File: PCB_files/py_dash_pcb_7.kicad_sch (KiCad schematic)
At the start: 5 parts, among them U1 CM4102008

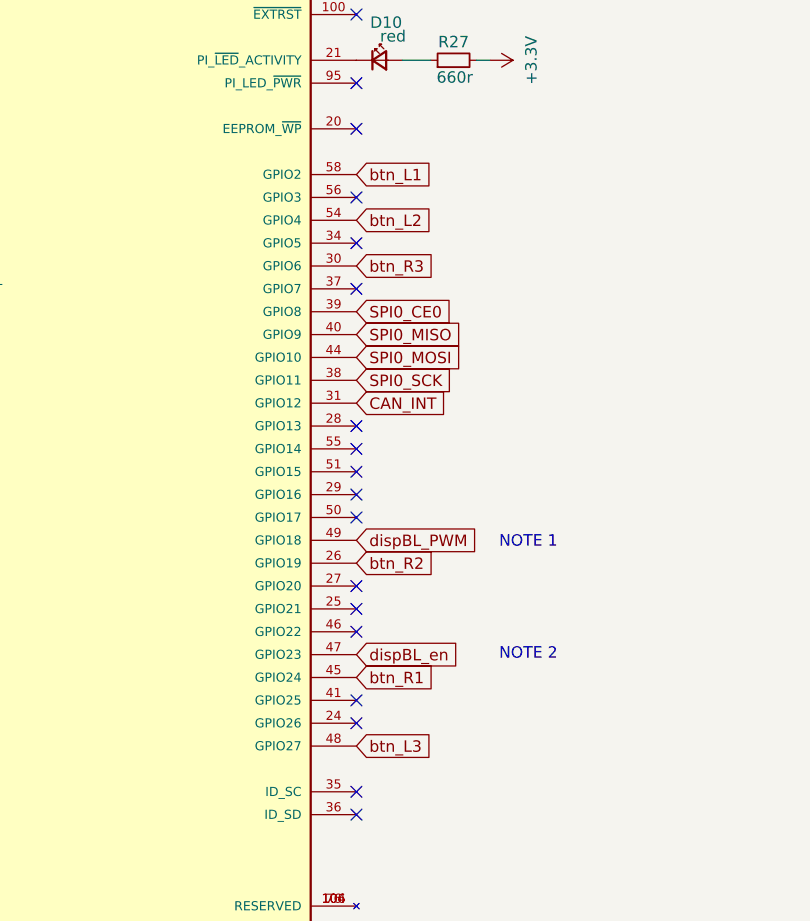
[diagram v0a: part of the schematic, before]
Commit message: r1a upload
uploaded files for r1a; correct button numbering
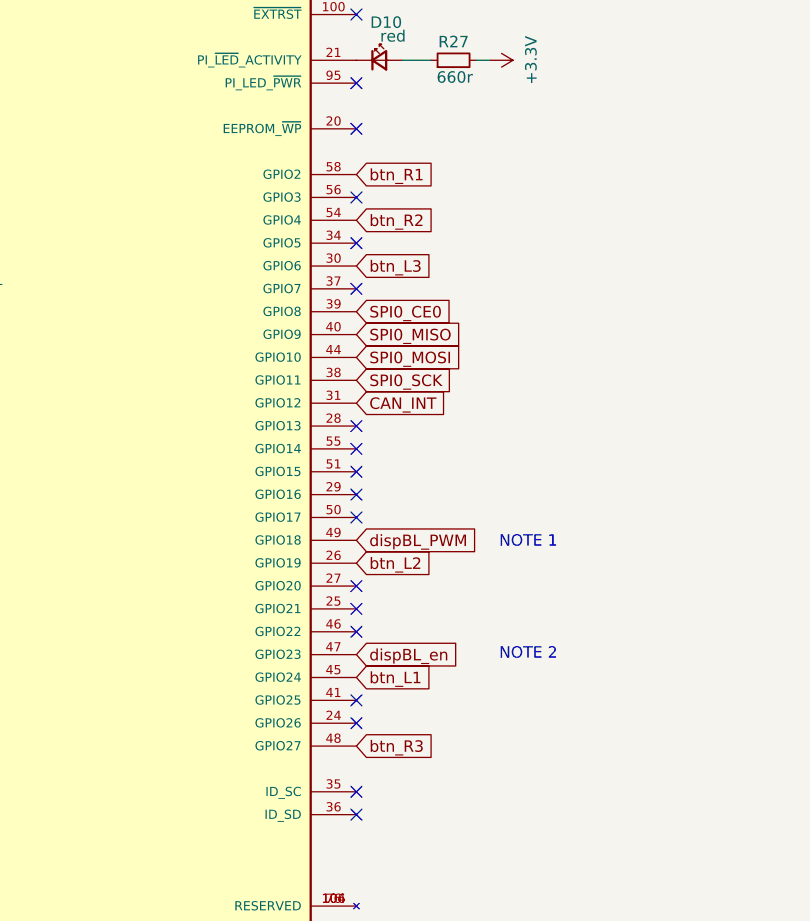
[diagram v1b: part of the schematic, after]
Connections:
- net btn_L1: now also U1.45 (GPIO24); no longer U1.58 (GPIO2)
- net btn_L2: now also U1.26 (GPIO19); no longer U1.54 (GPIO4)
- net btn_L3: now also U1.30 (GPIO6); no longer U1.48 (GPIO27)
- net btn_R1: now also U1.58 (GPIO2); no longer U1.45 (GPIO24)
- net btn_R2: now also U1.54 (GPIO4); no longer U1.26 (GPIO19)
- net btn_R3: now also U1.48 (GPIO27); no longer U1.30 (GPIO6)

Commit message: Rev2a initial upload
PCB files
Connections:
- net USB_OTG is gone; now on net GND: U1.101 (USB_OTG_ID)
- net SD_DET: now reaches U1.24 (GPIO26)
- net SD_CLK: now reaches U1.57 (SD_CLK)
- net SD_DAT3: now reaches U1.61 (SD_DAT3)
- net SD_CMD: now reaches U1.62 (SD_CMD)
- net SD_DAT0: now reaches U1.63 (SD_DAT0)
- net SD_DAT1: now reaches U1.67 (SD_DAT1)
- net SD_DAT2: now reaches U1.69 (SD_DAT2)
- net USBD+ renamed ext_USBD+
- net USBD- renamed ext_USBD-
- no-connect marks 104 -> 97

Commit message: push from desktop to align files
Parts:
- renumbered C33 to C1, C32 to C2, D10 to D1, R27 to R1
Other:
- added sheet mechanical (mechanical.kicad_sch)
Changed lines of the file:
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@@
 		(on_board yes)
 		(dnp no)
-		(property "Reference" "#PWR0101"
+		(property "Reference" "#PWR01"
 			(at 105.41 27.94 0)
 			(effects
@@
 			(project "py_dash_pcb_7"
 				(path "/84878699-1e21-48de-ad1b-9d4034e33e81"
-					(reference "#PWR0101")
+					(reference "#PWR01")
 					(unit 1)
 				)
@@
 		(on_board yes)
 		(dnp no)
-		(property "Reference" "D10"
+		(property "Reference" "D1"
 			(at 112.522 41.529 0)
 			(effects
@@
 			(project "py_dash_pcb_7"
 				(path "/84878699-1e21-48de-ad1b-9d4034e33e81"
-					(reference "D10")
+					(reference "D1")
 					(unit 1)
 				)
@@
 		(dnp no)
 		(fields_autoplaced yes)
-		(property "Reference" "#PWR0102"
+		(property "Reference" "#PWR08"
 			(at 92.837 178.562 0)
 			(effects
@@
 			(project "py_dash_pcb_7"
 				(path "/84878699-1e21-48de-ad1b-9d4034e33e81"
-					(reference "#PWR0102")
+					(reference "#PWR08")
 					(unit 1)
 				)
@@
 		(on_board yes)
 		(dnp no)
-		(property "Reference" "R27"
+		(property "Reference" "R1"
 			(at 120.015 43.688 90)
 			(effects
@@
 			(project "py_dash_pcb_7"
 				(path "/84878699-1e21-48de-ad1b-9d4034e33e81"
-					(reference "R27")
+					(reference "R1")
 					(unit 1)
 				)
@@
 		(dnp no)
 		(fields_autoplaced yes)
-		(property "Reference" "#PWR0105"
+		(property "Reference" "#PWR03"
 			(at 120.269 45.72 0)
 			(effects
@@
 			(project "py_dash_pcb_7"
 				(path "/84878699-1e21-48de-ad1b-9d4034e33e81"
-					(reference "#PWR0105")
+					(reference "#PWR03")
 					(unit 1)
 				)
@@
 		(on_board yes)
 		(dnp no)
-		(property "Reference" "#PWR0108"
+		(property "Reference" "#PWR05"
 			(at 41.91 55.88 0)
 			(effects
@@
 			(project "py_dash_pcb_7"
 				(path "/84878699-1e21-48de-ad1b-9d4034e33e81"
-					(reference "#PWR0108")
+					(reference "#PWR05")
 					(unit 1)
 				)
@@
 		(on_board yes)
 		(dnp no)
-		(property "Reference" "C32"
+		(property "Reference" "C2"
 			(at 88.3412 166.2176 0)
 			(effects
@@
 			(project "py_dash_pcb_7"
 				(path "/84878699-1e21-48de-ad1b-9d4034e33e81"
-					(reference "C32")
+					(reference "C2")
 					(unit 1)
 				)
@@
 		(on_board yes)
 		(dnp no)
-		(property "Reference" "C33"
+		(property "Reference" "C1"
 			(at 95.1738 162.4076 0)
 			(effects
@@
 			(project "py_dash_pcb_7"
 				(path "/84878699-1e21-48de-ad1b-9d4034e33e81"
-					(reference "C33")
+					(reference "C1")
 					(unit 1)
 				)
@@
 		(dnp no)
 		(fields_autoplaced yes)
-		(property "Reference" "#PWR02"
+		(property "Reference" "#PWR06"
 			(at 115.57 144.78 0)
 			(effects
@@
 			(project "py_dash_pcb_7"
 				(path "/84878699-1e21-48de-ad1b-9d4034e33e81"
-					(reference "#PWR02")
+					(reference "#PWR06")
 					(unit 1)
 				)
@@
 		(on_board yes)
 		(dnp no)
-		(property "Reference" "#PWR0103"
+		(property "Reference" "#PWR07"
 			(at 86.106 163.703 0)
 			(effects
@@
 			(project "py_dash_pcb_7"
 				(path "/84878699-1e21-48de-ad1b-9d4034e33e81"
-					(reference "#PWR0103")
+					(reference "#PWR07")
 					(unit 1)
 				)
@@
 		(on_board yes)
 		(dnp no)
-		(property "Reference" "#PWR0107"
+		(property "Reference" "#PWR04"
 			(at 41.91 53.34 0)
 			(effects
@@
 			(project "py_dash_pcb_7"
 				(path "/84878699-1e21-48de-ad1b-9d4034e33e81"
-					(reference "#PWR0107")
+					(reference "#PWR04")
 					(unit 1)
 				)
@@
 		(dnp no)
 		(fields_autoplaced yes)
-		(property "Reference" "#PWR03"
+		(property "Reference" "#PWR02"
 			(at 171.45 38.1 0)
 			(effects
@@
 			(project "py_dash_pcb_7"
 				(path "/84878699-1e21-48de-ad1b-9d4034e33e81"
-					(reference "#PWR03")
+					(reference "#PWR02")
 					(unit 1)
 				)
@@
 	)
 	(sheet
-		(at 232.41 170.18)
+		(at 253.365 170.307)
 		(size 12.7 3.81)
 		(exclude_from_sim no)
@@
 			(color 0 0 0 0.0000)
 		)
+		(property "Sheetname" "mechanical"
+			(at 253.365 169.5954 0)
+			(effects
+				(font
+					(size 1.27 1.27)
+				)
+				(justify left bottom)
+			)
+		)
+		(property "Sheetfile" "mechanical.kicad_sch"
+			(at 253.365 174.7016 0)
+			(effects
+				(font
+					(size 1.27 1.27)
+				)
+				(justify left top)
+			)
+		)
+		(instances
+			(project "py_dash_pcb_7"
+				(path "/84878699-1e21-48de-ad1b-9d4034e33e81"
+					(page "5")
+				)
+			)
+		)
+	)
+	(sheet
+		(at 230.124 170.18)
+		(size 12.7 3.81)
+		(exclude_from_sim no)
+		(in_bom yes)
+		(on_board yes)
+		(dnp no)
+		(fields_autoplaced yes)
+		(stroke
+			(width 0.1524)
+			(type solid)
+		)
+		(fill
+			(color 0 0 0 0.0000)
+		)
 		(property "Sheetname" "perif"
-			(at 232.41 169.4684 0)
+			(at 230.124 169.4684 0)
 			(effects
 				(font
@@
 		)
 		(property "Sheetfile" "perif.kicad_sch"
-			(at 232.41 174.5746 0)
-			(effects
-				(font
+			(at 230.124 174.5746 0)
+			(effects
+				(font

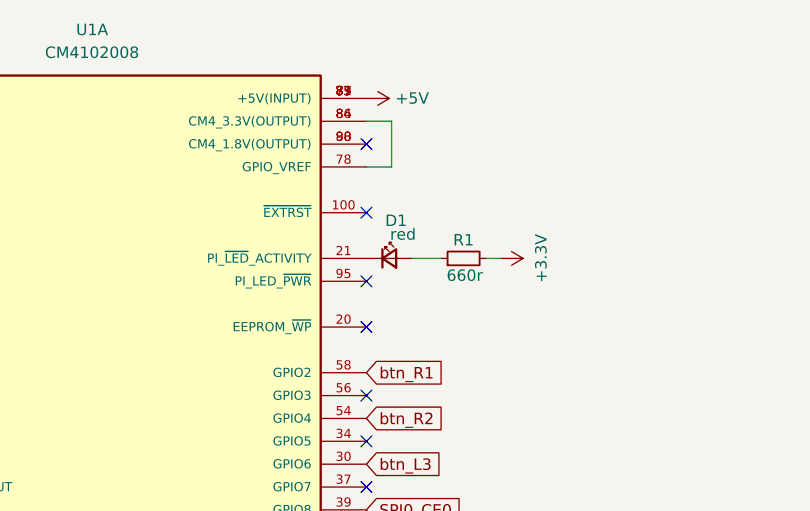
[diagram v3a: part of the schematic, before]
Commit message: final BOM and tweaking
Tweaked some dimensions after mechanical assembly. Generated BOM and reviewed against reseller inventory
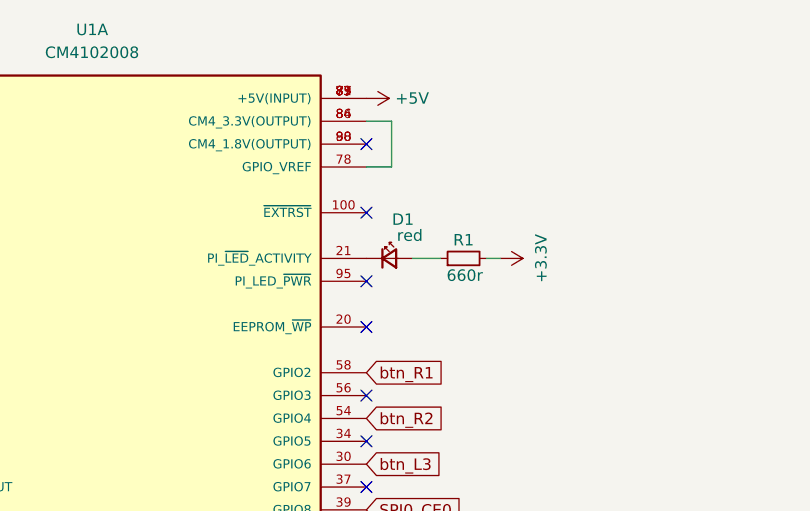
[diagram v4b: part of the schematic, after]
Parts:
- C1: MPN (none) -> C0805C105M3RACTU; Manufacturer (none) -> Kemet; Mouser_PN 80-C0805C105M3R -> (none); Reseller_P/N (none) -> 80-C0805C105M3R; Source/Reseller (none) -> Mouser
- C2: MPN (none) -> T495B106K025ATE750; Manufacturer (none) -> Kemet; Mouser_PN 80-T495B106K25ATE750 -> (none); Reseller_P/N (none) -> 80-T495B106K25ATE750; Source/Reseller (none) -> Mouser
- D1: MPN (none) -> 150080RS75000; Manufacturer (none) -> Wurth; Mouser_PN 710-150080RS75000 -> (none); Reseller_P/N (none) -> 710-150080RS75000; Source/Reseller (none) -> Mouser
- R1: MPN (none) -> CRCW0805665RFKEA; Manufacturer (none) -> Vishay; Mouser_PN 71-CRCW0805-665-E3 -> (none); Reseller_P/N (none) -> 71-CRCW0805-665-E3; Source/Reseller (none) -> Mouser
- U1: MPN (none) -> CM4001008; Manufacturer (none) -> Raspberry PI; Mouser_PN N/A -> (none); Reseller_P/N (none) -> 2648-SC0696-ND; Source/Reseller (none) -> Digikey
